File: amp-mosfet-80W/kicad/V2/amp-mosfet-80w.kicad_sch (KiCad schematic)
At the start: 60 parts, among them J1 Conn_01x01, J2 Conn_01x01, J3 +50V, J4 -50V, J5 LS+, J6 LS-, J7 GND, Q1 BC856BS, Q11 ECX10P20, Q12 ECX10N20, Q2 BC856BS, Q3 DZT5551, Q4 DZT5401, Q5 DZT5401, Q6 DZT5551

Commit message: Change some values
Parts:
- R4, R7: value 3k9 -> 4k7
- R5: value 430R -> 680R
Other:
- note added: "I:1mA"
- note removed: "I:1.7mA = > 430R"
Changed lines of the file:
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@@
   (title_block
     (title "Lateral MOS FET 80W")
-    (date "2021-12-28")
+    (date "2022-01-03")
     (rev "V2")
   )
@@
     (effects (font (size 1.27 1.27)) (justify left bottom))
   )
-  (text "I:1.7mA = > 430R" (at 86.36 73.66 0)
+  (text "I:1mA" (at 86.36 73.66 0)
     (effects (font (size 1.27 1.27)) (justify left bottom))
   )
@@
       (effects (font (size 1.27 1.27)) (justify left))
     )
-    (property "Value" "430R" (id 1) (at 86.868 68.453 0)
+    (property "Value" "680R" (id 1) (at 86.868 68.453 0)
       (effects (font (size 1.27 1.27)) (justify left))
     )
@@
       (effects (font (size 1.27 1.27)) (justify left))
     )
-    (property "Value" "3k9" (id 1) (at 95.758 209.423 0)
+    (property "Value" "4k7" (id 1) (at 95.758 209.423 0)
       (effects (font (size 1.27 1.27)) (justify left))
     )
@@
       (effects (font (size 1.27 1.27)) (justify left))
     )
-    (property "Value" "3k9" (id 1) (at 77.978 209.423 0)
+    (property "Value" "4k7" (id 1) (at 77.978 209.423 0)
       (effects (font (size 1.27 1.27)) (justify left))
     )
@@
     )
     (path "/00000000-0000-0000-0000-000061935443"
-      (reference "R4") (unit 1) (value "3k9") (footprint "Resistor_SMD:R_0805_2012Metric_Pad1.20x1.40mm_HandSolder")
+      (reference "R4") (unit 1) (value "4k7") (footprint "Resistor_SMD:R_0805_2012Metric_Pad1.20x1.40mm_HandSolder")
     )
     (path "/00000000-0000-0000-0000-00006192531f"
-      (reference "R5") (unit 1) (value "430R") (footprint "Resistor_SMD:R_0805_2012Metric_Pad1.20x1.40mm_HandSolder")
+      (reference "R5") (unit 1) (value "680R") (footprint "Resistor_SMD:R_0805_2012Metric_Pad1.20x1.40mm_HandSolder")
     )
     (path "/00000000-0000-0000-0000-00006191f500"
@@
     )
     (path "/00000000-0000-0000-0000-000061934148"
-      (reference "R7") (unit 1) (value "3k9") (footprint "Resistor_SMD:R_0805_2012Metric_Pad1.20x1.40mm_HandSolder")
+      (reference "R7") (unit 1) (value "4k7") (footprint "Resistor_SMD:R_0805_2012Metric_Pad1.20x1.40mm_HandSolder")
     )
     (path "/00000000-0000-0000-0000-000061927938"

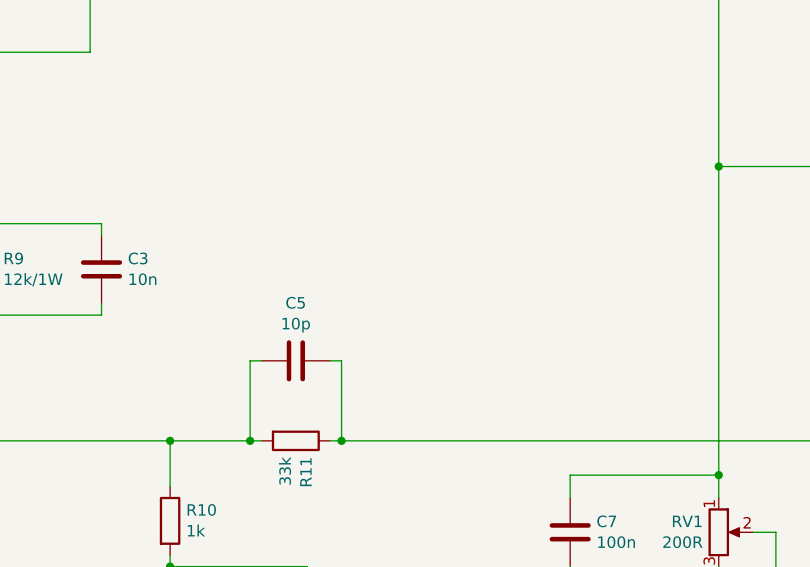
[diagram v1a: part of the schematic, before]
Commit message: Update amp-mosfet-80w.kicad_sch
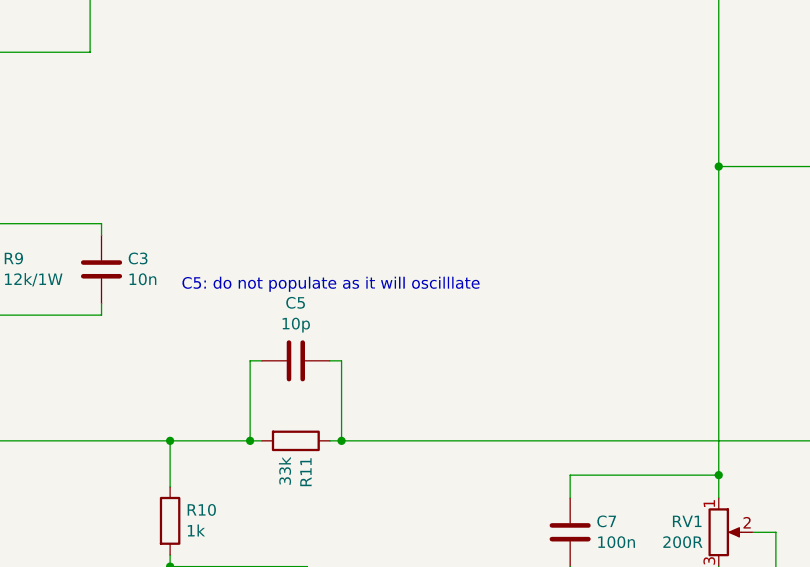
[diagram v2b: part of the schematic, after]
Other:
- note added: "C5: do not populate as it will oscilllate"
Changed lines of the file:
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@@
   (title_block
     (title "Lateral MOS FET 80W")
-    (date "2022-01-03")
+    (date "2022-01-05")
     (rev "V2")
   )
@@
     (stroke (width 0) (type default) (color 0 0 0 0))
   )
+  (text "C5: do not populate as it will oscilllate" (at 130.81 119.38 0)
+    (effects (font (size 1.27 1.27)) (justify left bottom))
+  )
   (text "Idle: 100mA" (at 279.4 67.31 0)
